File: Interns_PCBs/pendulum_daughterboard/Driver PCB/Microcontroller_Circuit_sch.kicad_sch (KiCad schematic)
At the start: 5 parts, among them J1 AVR-ISP-6, SW1 SW_Push, U10 ATtiny85-20S

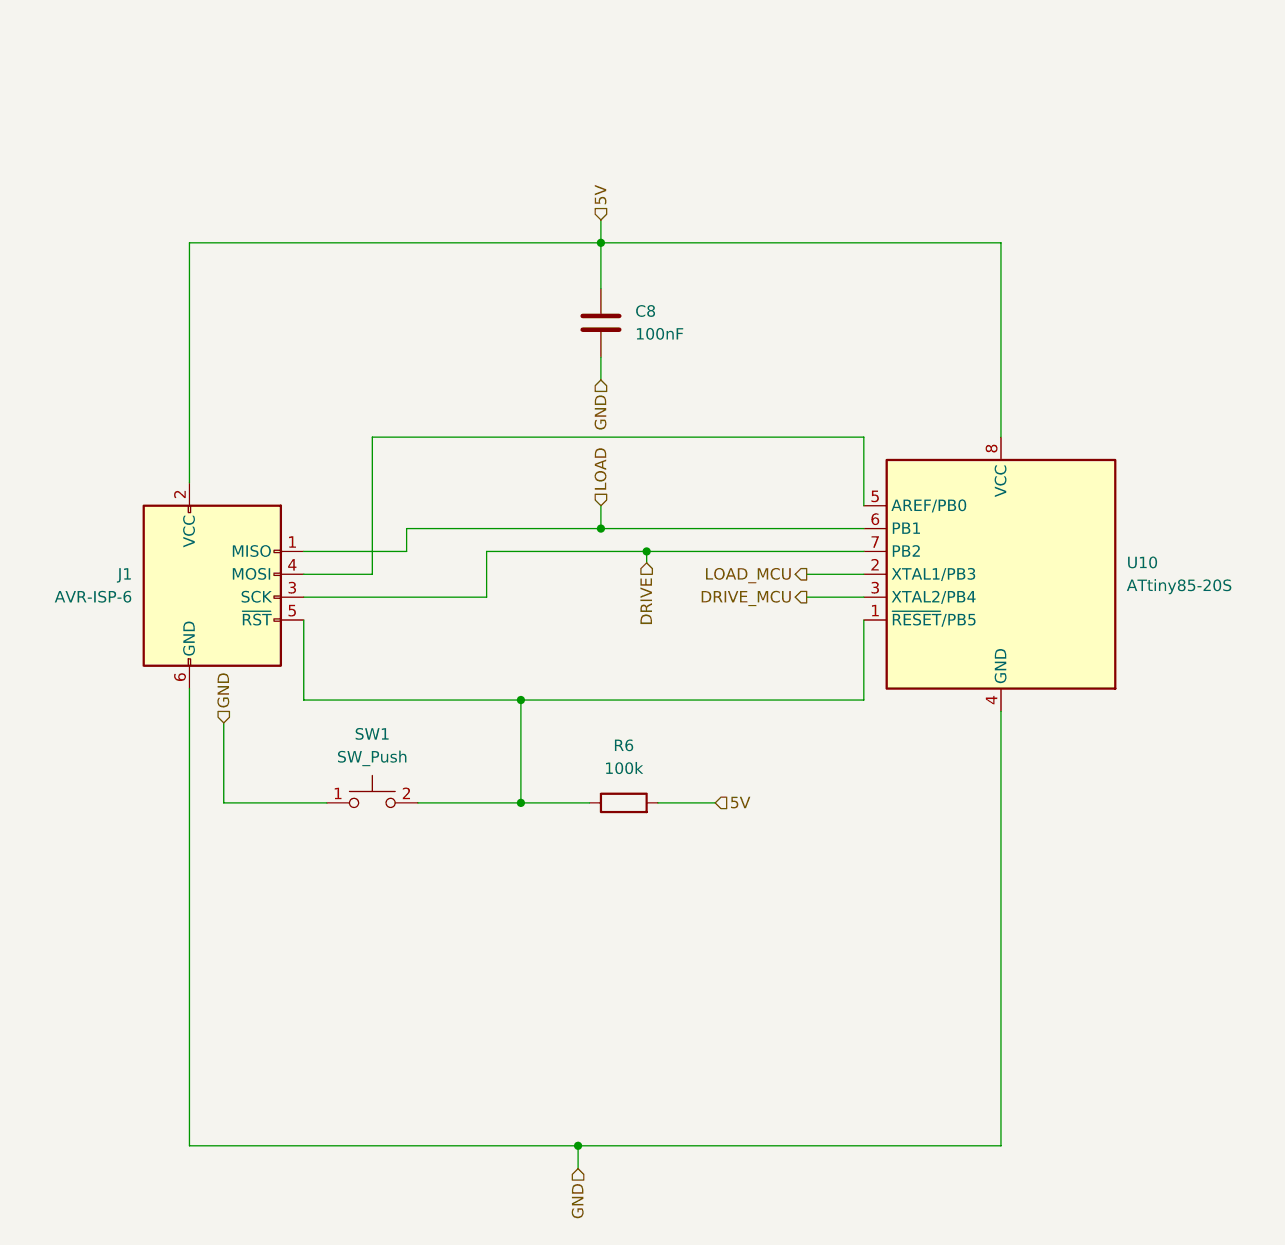
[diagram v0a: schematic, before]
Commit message: Pull down and Current Limiting Resistors
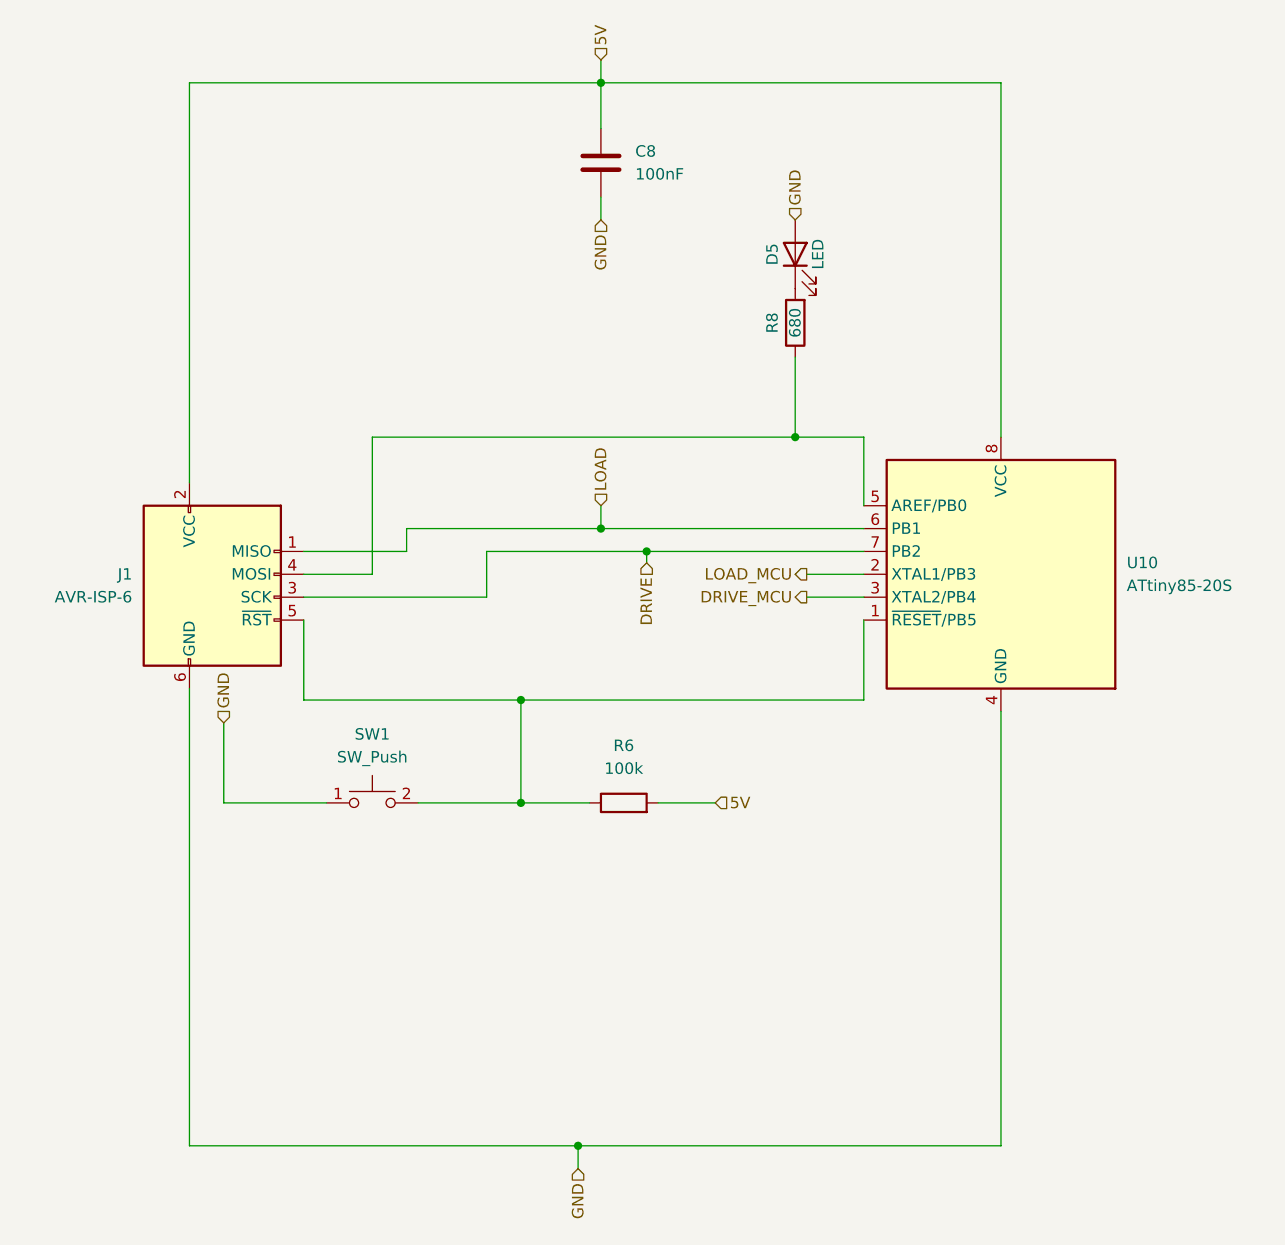
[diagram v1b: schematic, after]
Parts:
- added D5: LED, LED_SMD:LED_0805_2012Metric_Pad1.15x1.40mm_HandSolder, symbol Device:LED
- added R8: 680, Resistor_SMD:R_0805_2012Metric_Pad1.20x1.40mm_HandSolder, symbol Device:R
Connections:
- net GND: now also D5.2 (A)
- net at J1.4 (MOSI), U10.5 (AREF/PB0): now also R8.1
- new net: D5.1 (K), R8.2
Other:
- moved on the sheet: C8
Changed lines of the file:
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@@
   (junction (at 137.16 113.03) (diameter 0) (color 0 0 0 0)
   )
+  (junction (at 167.64 72.39) (diameter 0) (color 0 0 0 0)
+  )
   (junction (at 151.13 85.09) (diameter 0) (color 0 0 0 0)
   )
   (junction (at 146.05 82.55) (diameter 0) (color 0 0 0 0)
   )
-  (junction (at 146.05 50.8) (diameter 0) (color 0 0 0 0)
+  (junction (at 146.05 33.02) (diameter 0) (color 0 0 0 0)
   )
   (junction (at 143.51 151.13) (diameter 0) (color 0 0 0 0)
@@
     (stroke (width 0) (type default) (color 0 0 0 0))
   )
-  (wire (pts (xy 100.33 50.8) (xy 146.05 50.8))
+  (wire (pts (xy 100.33 33.02) (xy 146.05 33.02))
     (stroke (width 0) (type default) (color 0 0 0 0))
   )
@@
     (stroke (width 0) (type default) (color 0 0 0 0))
   )
-  (wire (pts (xy 146.05 50.8) (xy 146.05 55.88))
+  (wire (pts (xy 146.05 33.02) (xy 146.05 38.1))
     (stroke (width 0) (type default) (color 0 0 0 0))
   )
@@
     (stroke (width 0) (type default) (color 0 0 0 0))
   )
+  (wire (pts (xy 167.64 72.39) (xy 175.26 72.39))
+    (stroke (width 0) (type default) (color 0 0 0 0))
+  )
   (wire (pts (xy 133.35 90.17) (xy 133.35 85.09))
     (stroke (width 0) (type default) (color 0 0 0 0))
@@
     (stroke (width 0) (type default) (color 0 0 0 0))
   )
-  (wire (pts (xy 100.33 77.47) (xy 100.33 50.8))
+  (wire (pts (xy 100.33 77.47) (xy 100.33 33.02))
     (stroke (width 0) (type default) (color 0 0 0 0))
   )
@@
     (stroke (width 0) (type default) (color 0 0 0 0))
   )
-  (wire (pts (xy 146.05 48.26) (xy 146.05 50.8))
+  (wire (pts (xy 167.64 63.5) (xy 167.64 72.39))
+    (stroke (width 0) (type default) (color 0 0 0 0))
+  )
+  (wire (pts (xy 146.05 30.48) (xy 146.05 33.02))
     (stroke (width 0) (type default) (color 0 0 0 0))
   )
@@
     (stroke (width 0) (type default) (color 0 0 0 0))
   )
-  (wire (pts (xy 146.05 63.5) (xy 146.05 66.04))
+  (wire (pts (xy 146.05 45.72) (xy 146.05 48.26))
     (stroke (width 0) (type default) (color 0 0 0 0))
   )
@@
     (stroke (width 0) (type default) (color 0 0 0 0))
   )
-  (wire (pts (xy 146.05 50.8) (xy 190.5 50.8))
-    (stroke (width 0) (type default) (color 0 0 0 0))
-  )
-  (wire (pts (xy 190.5 50.8) (xy 190.5 72.39))
+  (wire (pts (xy 146.05 33.02) (xy 190.5 33.02))
+    (stroke (width 0) (type default) (color 0 0 0 0))
+  )
+  (wire (pts (xy 190.5 33.02) (xy 190.5 72.39))
     (stroke (width 0) (type default) (color 0 0 0 0))
   )
@@
     (stroke (width 0) (type default) (color 0 0 0 0))
   )
-  (wire (pts (xy 120.65 72.39) (xy 175.26 72.39))
+  (wire (pts (xy 120.65 72.39) (xy 167.64 72.39))
     (stroke (width 0) (type default) (color 0 0 0 0))
   )
@@
     (effects (font (size 1.27 1.27)) (justify right))
   )
+  (hierarchical_label "GND" (shape input) (at 167.64 48.26 90)
+    (effects (font (size 1.27 1.27)) (justify left))
+  )
   (hierarchical_label "5V" (shape input) (at 158.75 113.03 0)
     (effects (font (size 1.27 1.27)) (justify left))
@@
     (effects (font (size 1.27 1.27)) (justify right))
   )
-  (hierarchical_label "GND" (shape input) (at 146.05 66.04 270)
+  (hierarchical_label "GND" (shape input) (at 146.05 48.26 270)
     (effects (font (size 1.27 1.27)) (justify right))
   )
@@
     (effects (font (size 1.27 1.27)) (justify left))
   )
-  (hierarchical_label "5V" (shape input) (at 146.05 48.26 90)
+  (hierarchical_label "5V" (shape input) (at 146.05 30.48 90)
     (effects (font (size 1.27 1.27)) (justify left))
   )
@@
     (pin "8")
   )
-  (symbol (lib_id "Device:C") (at 146.05 59.69 0) (unit 1)
-    (in_bom yes) (on_board yes) (fields_autoplaced)
-    (property "Reference" "C8" (id 0) (at 149.86 58.4199 0)
+  (symbol (lib_id "Device:R") (at 167.64 59.69 180) (unit 1)
+    (in_bom yes) (on_board yes)
+    (property "Reference" "R8" (id 0) (at 165.1 59.69 90))
+    (property "Value" "680" (id 1) (at 167.64 59.69 90))
+    (property "Footprint" "Resistor_SMD:R_0805_2012Metric_Pad1.20x1.40mm_HandSolder" (id 2) (at 169.418 59.69 90)
+      (effects (font (size 1.27 1.27)) hide)
+    )
+    (property "Datasheet" "~" (id 3) (at 167.64 59.69 0)
+      (effects (font (size 1.27 1.27)) hide)
+    )
+    (pin "1")
+    (pin "2")
+  )
+  (symbol (lib_id "Device:C") (at 146.05 41.91 0) (unit 1)
+    (in_bom yes) (on_board yes) (fields_autoplaced)
+    (property "Reference" "C8" (id 0) (at 149.86 40.6399 0)
       (effects (font (size 1.27 1.27)) (justify left))
     )
-    (property "Value" "100nF" (id 1) (at 149.86 60.9599 0)
+    (property "Value" "100nF" (id 1) (at 149.86 43.1799 0)
       (effects (font (size 1.27 1.27)) (justify left))
     )
-    (property "Footprint" "Capacitor_SMD:C_0805_2012Metric_Pad1.18x1.45mm_HandSolder" (id 2) (at 147.0152 63.5 0)
-      (effects (font (size 1.27 1.27)) hide)
-    )
-    (property "Datasheet" "~" (id 3) (at 146.05 59.69 0)
+    (property "Footprint" "Capacitor_SMD:C_0805_2012Metric_Pad1.18x1.45mm_HandSolder" (id 2) (at 147.0152 45.72 0)
+      (effects (font (size 1.27 1.27)) hide)
+    )
+    (property "Datasheet" "~" (id 3) (at 146.05 41.91 0)
       (effects (font (size 1.27 1.27)) hide)
     )
@@
       (effects (font (size 1.27 1.27)) hide)
     )
+    (pin "1")
+    (pin "2")
+  )
+  (symbol (lib_id "Device:LED") (at 167.64 52.07 90) (unit 1)
+    (in_bom yes) (on_board yes)
+    (property "Reference" "D5" (id 0) (at 165.1 52.07 0))
+    (property "Value" "LED" (id 1) (at 170.18 52.07 0))
+    (property "Footprint" "LED_SMD:LED_0805_2012Metric_Pad1.15x1.40mm_HandSolder" (id 2) (at 167.64 52.07 0)
+      (effects (font (size 1.27 1.27)) hide)
+    )
+    (property "Datasheet" "~" (id 3) (at 167.64 52.07 0)
+      (effects (font (size 1.27 1.27)) hide)
+    )
